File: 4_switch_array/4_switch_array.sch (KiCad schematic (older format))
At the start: 17 parts, among them J1 Conn_01x04, J2 Conn_01x04, J3 Conn_01x02, J4 Conn_01x02, J5 Conn_01x02, J6 Conn_01x02, J7 Conn_01x02, Q1 Q_NPN_EBC, Q2 Q_NPN_EBC, Q3 Q_NPN_EBC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

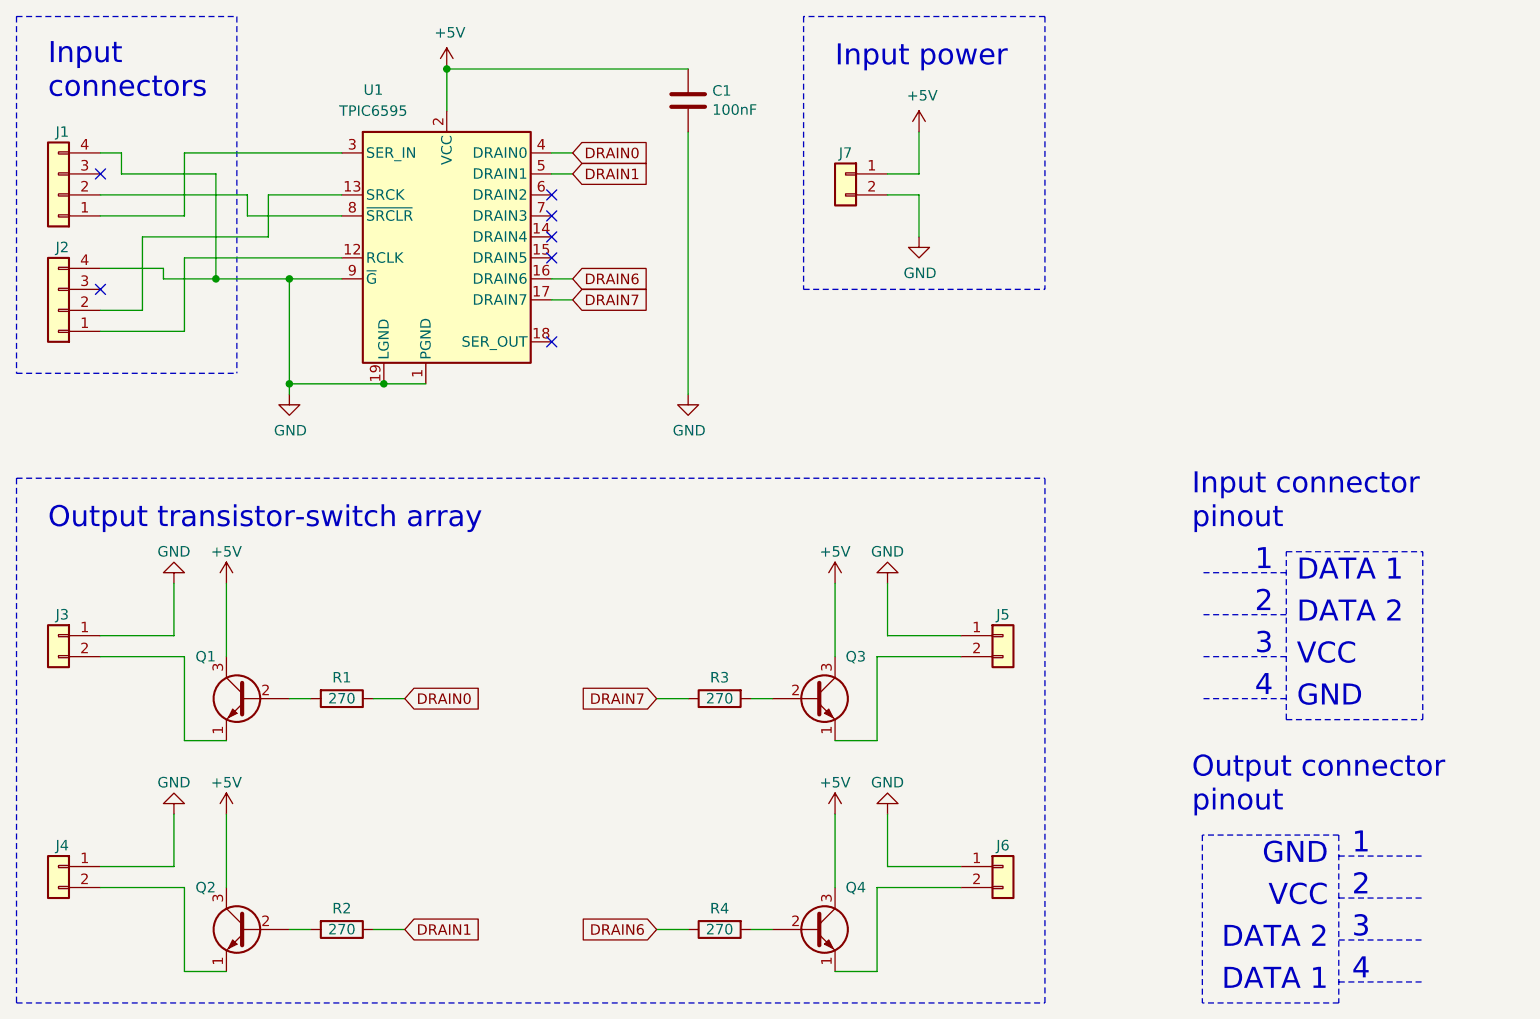
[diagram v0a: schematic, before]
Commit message: Changed pinout to VCC-GND
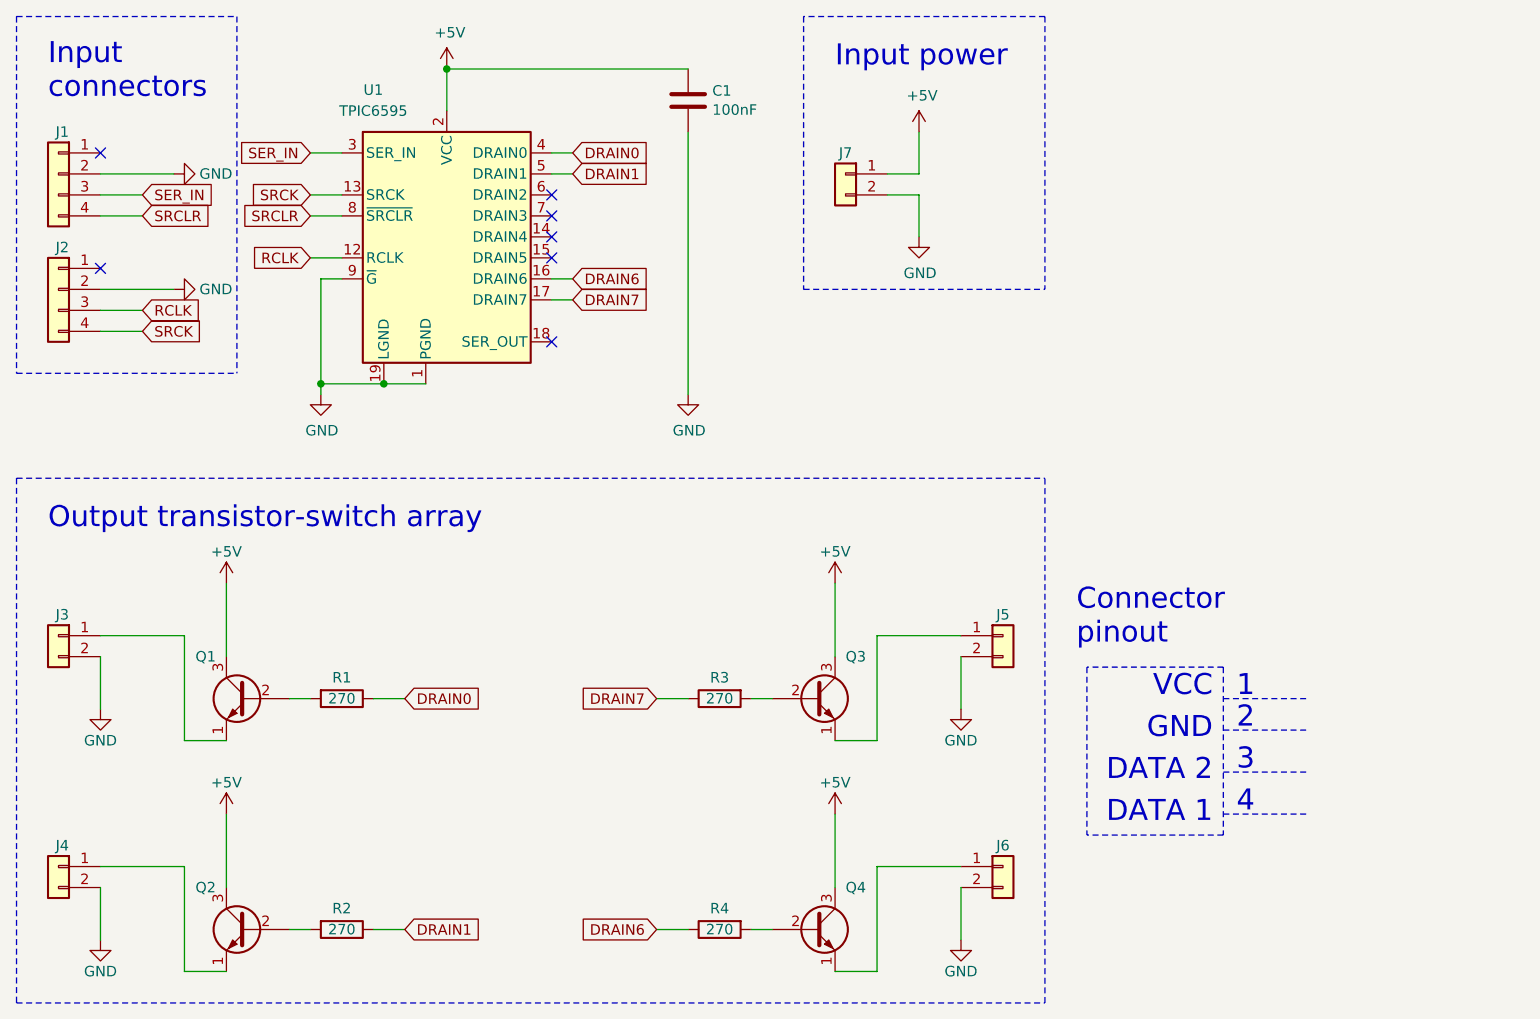
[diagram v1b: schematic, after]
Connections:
- net GND: now also J1.2 (Pin_2), J2.2 (Pin_2), J3.2 (Pin_2), J4.2 (Pin_2), J5.2 (Pin_2), J6.2 (Pin_2); no longer J1.4 (Pin_4), J2.4 (Pin_4), J3.1 (Pin_1), J4.1 (Pin_1), J5.1 (Pin_1), J6.1 (Pin_1)
- net at Q4.1 (E): now also J6.1 (Pin_1); no longer J6.2 (Pin_2)
- net at J1.1 (Pin_1): no longer U1.3 (SER_IN)
- net SRCLR: now reaches U1.8 (~SRCLR)
- net SRCLR: now also J1.4 (Pin_4); no longer J1.2 (Pin_2)
- net SER_IN: now reaches J1.3 (Pin_3)
- net SER_IN: now also U1.3 (SER_IN)
- net at J2.1 (Pin_1): no longer U1.12 (RCLK)
- net SRCK: now reaches U1.13 (SRCK)
- net SRCK: now also J2.4 (Pin_4); no longer J2.2 (Pin_2)
- net RCLK: now reaches J2.3 (Pin_3)
- net RCLK: now also U1.12 (RCLK)
- net at Q3.1 (E): now also J5.1 (Pin_1); no longer J5.2 (Pin_2)
- net at Q2.1 (E): now also J4.1 (Pin_1); no longer J4.2 (Pin_2)
- net at Q1.1 (E): now also J3.1 (Pin_1); no longer J3.2 (Pin_2)
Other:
- note added: "Connector\npinout"
- note removed: "Input connector\npinout"
- note removed: "Output connector\npinout"
